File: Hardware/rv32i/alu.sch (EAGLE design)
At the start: 51 parts, among them IC1 SN74HCS86DR, IC10 SN74HCS86DR, IC11 SN74HCS86DR, IC12 SN74HCS86DR, IC13 SN74HCS86DR, IC14 SN74HCS86DR, IC15 SN74HCS86DR, IC16 SN74HCS86DR, IC17 SN74HCS86DR, IC18 SN74HCS86DR, IC19 SN74HCS86DR, IC2 SN74HCS86DR, IC20 SN74HCS86DR, IC21 SN74HCS86DR, IC22 SN74HCS86DR, IC23 SN74HCS86DR, IC24 SN74HCS86DR, IC25 SN74ACT08D, IC26 SN74ACT08D, IC27 SN74ACT08D, IC28 SN74ACT08D, IC29 SN74ACT08D, IC3 SN74HCS86DR, IC30 SN74ACT08D, IC31 SN74ACT08D, IC32 SN74ACT08D, IC33 SN74ACT08D, IC34 SN74ACT08D, IC35 SN74ACT08D, IC36 SN74ACT08D, IC37 SN74ACT08D, IC38 SN74ACT08D, IC39 SN74ACT08D, IC4 SN74HCS86DR, IC40 SN74ACT08D, IC41 SN74HCS32DR, IC42 SN74HCS32DR, IC43 SN74HCS32DR, IC44 SN74HCS32DR, IC45 SN74HCS32DR, IC46 SN74HCS32DR, IC47 SN74HCS32DR, IC48 SN74HCS32DR, IC5 SN74HCS86DR, IC6 SN74HCS86DR, IC7 SN74HCS86DR, IC8 SN74HCS86DR, IC9 SN74HCS86DR

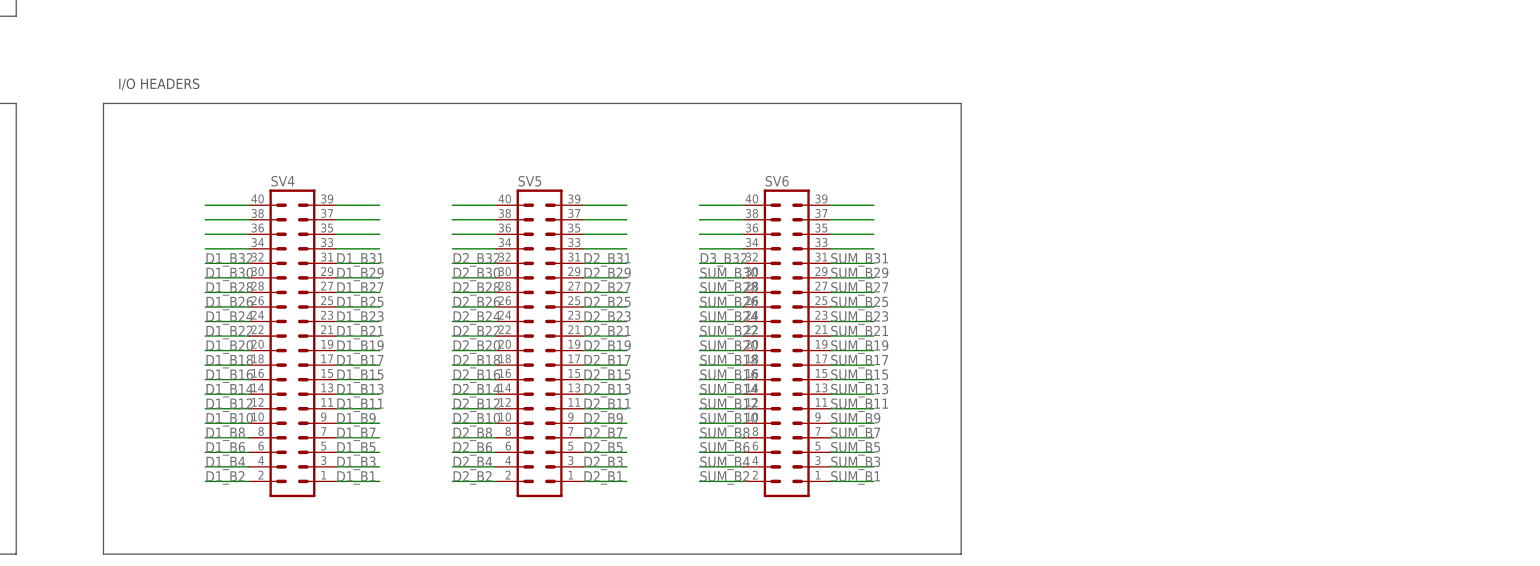
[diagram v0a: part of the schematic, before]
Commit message: Headers Changed
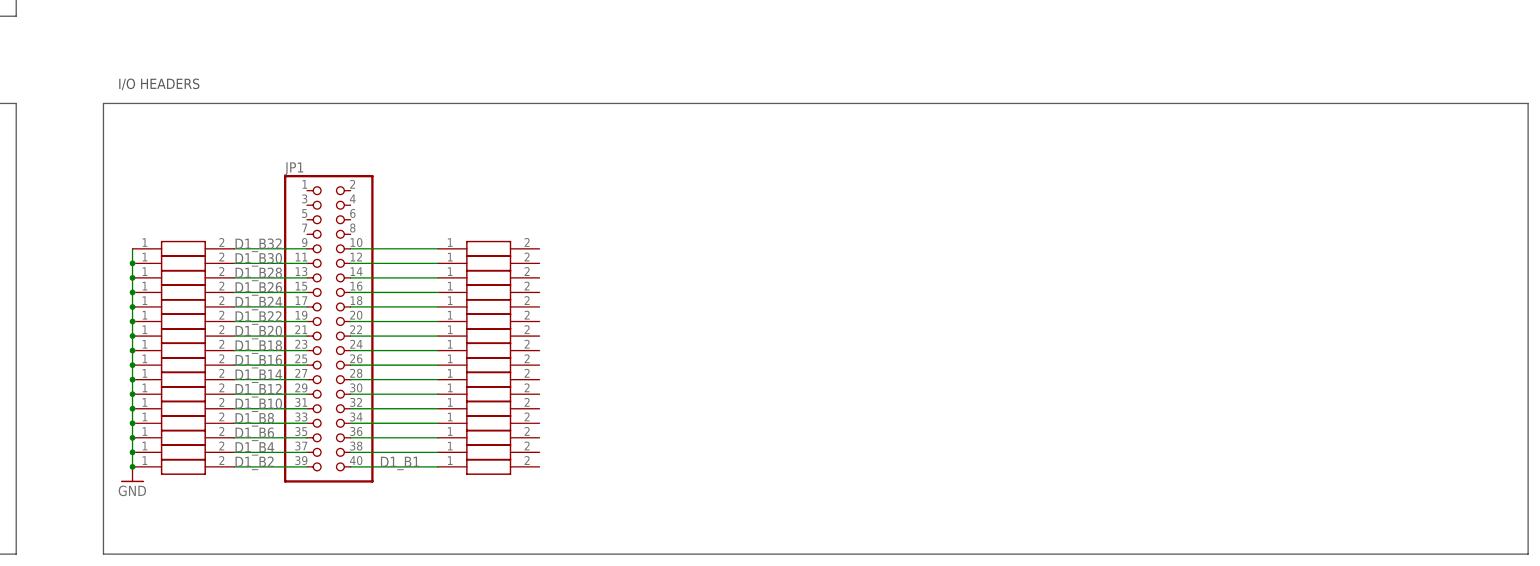
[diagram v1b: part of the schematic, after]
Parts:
- removed SV4, SV5, SV6: (no value), con-lstb:MA20-2
- added JP1: (no value), pinhead:PINHD-2X20
- added R1, R10, R11, R12, R13, R14, R15, R16, R17, R18, R19, R2, R20, R21, R22, R23, R24, R25, R26, R27, R28, R29, R3, R30, R31, R32, R4, R5, R6, R7, R8, R9: RC0603FR-0710KL, RC0603FR-0710KL:RC0603FR-0710KL
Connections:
- removed net B1_A0: SV4.33
- removed net D1_B34: SV4.34
- removed net D3_B32: SV6.32
- removed net N$569: SV4.38
- removed net N$570: SV4.36
- removed net N$587: SV4.37
- removed net N$588: SV4.35
- removed net N$607: SV4.39
- removed net N$608: SV4.40
- removed net N$609: SV5.38
- removed net N$610: SV5.36
- removed net N$611: SV5.34
- removed net N$627: SV5.37
- removed net N$628: SV5.35
- removed net N$629: SV5.33
- removed net N$647: SV5.39
- removed net N$648: SV5.40
- removed net N$649: SV6.38
- removed net N$650: SV6.36
- removed net N$651: SV6.34
- removed net N$667: SV6.37
- removed net N$668: SV6.35
- removed net N$669: SV6.33
- removed net N$687: SV6.39
- removed net N$688: SV6.40
- new net GND: R1.1, R10.1, R11.1, R12.1, R13.1, R14.1, R15.1, R16.1, R2.1, R3.1, R4.1, R5.1, R6.1, R7.1, R8.1, R9.1
- new net N$10: JP1.22, R26.1
- new net N$11: JP1.24, R25.1
- new net N$12: JP1.26, R17.1
- new net N$13: JP1.28, R18.1
- new net N$14: JP1.30, R19.1
- new net N$16: JP1.32, R20.1
- new net N$17: JP1.34, R22.1
- new net N$18: JP1.36, R21.1
- new net N$19: JP1.38, R23.1
- new net N$2: JP1.10, R31.1
- new net N$4: JP1.12, R32.1
- new net N$5: JP1.14, R30.1
- new net N$6: JP1.16, R29.1
- new net N$7: JP1.18, R28.1
- new net N$9: JP1.20, R27.1
- net D1_B1: now also JP1.40, R24.1; no longer SV4.1
- net D1_B10: now also JP1.31, R4.2; no longer SV4.10
- net D1_B11: no longer SV4.11
- net D1_B12: now also JP1.29, R3.2; no longer SV4.12
- net D1_B13: no longer SV4.13
- net D1_B14: now also JP1.27, R2.2; no longer SV4.14
- net D1_B15: no longer SV4.15
- net D1_B16: now also JP1.25, R1.2; no longer SV4.16
- net D1_B17: no longer SV4.17
- net D1_B18: now also JP1.23, R9.2; no longer SV4.18
- net D1_B19: no longer SV4.19
- net D1_B2: now also JP1.39, R8.2; no longer SV4.2
- net D1_B20: now also JP1.21, R10.2; no longer SV4.20
- net D1_B21: no longer SV4.21
- net D1_B22: now also JP1.19, R11.2; no longer SV4.22
- net D1_B23: no longer SV4.23
- net D1_B24: now also JP1.17, R12.2; no longer SV4.24
- net D1_B25: no longer SV4.25
- net D1_B26: now also JP1.15, R13.2; no longer SV4.26
- net D1_B27: no longer SV4.27
- net D1_B28: now also JP1.13, R14.2; no longer SV4.28
- net D1_B29: no longer SV4.29
- net D1_B3: no longer SV4.3
- net D1_B30: now also JP1.11, R16.2; no longer SV4.30
- net D1_B31: no longer SV4.31
- net D1_B32: now also JP1.9, R15.2; no longer SV4.32
- net D1_B4: now also JP1.37, R7.2; no longer SV4.4
- net D1_B5: no longer SV4.5
- net D1_B6: now also JP1.35, R5.2; no longer SV4.6
- net D1_B7: no longer SV4.7
- net D1_B8: now also JP1.33, R6.2; no longer SV4.8
- net D1_B9: no longer SV4.9
- net D2_B1: no longer SV5.1
- net D2_B10: no longer SV5.10
- net D2_B11: no longer SV5.11
- net D2_B12: no longer SV5.12
- net D2_B13: no longer SV5.13
- net D2_B14: no longer SV5.14
- net D2_B15: no longer SV5.15
- net D2_B16: no longer SV5.16
- net D2_B17: no longer SV5.17
- net D2_B18: no longer SV5.18
- net D2_B19: no longer SV5.19
- net D2_B2: no longer SV5.2
- net D2_B20: no longer SV5.20
- net D2_B21: no longer SV5.21
- net D2_B22: no longer SV5.22
- net D2_B23: no longer SV5.23
- net D2_B24: no longer SV5.24
- net D2_B25: no longer SV5.25
- net D2_B26: no longer SV5.26
- net D2_B27: no longer SV5.27
- net D2_B28: no longer SV5.28
- net D2_B29: no longer SV5.29
- net D2_B3: no longer SV5.3
- net D2_B30: no longer SV5.30
- net D2_B31: no longer SV5.31
- net D2_B32: no longer SV5.32
- net D2_B4: no longer SV5.4
- net D2_B5: no longer SV5.5
- net D2_B6: no longer SV5.6
- net D2_B7: no longer SV5.7
- net D2_B8: no longer SV5.8
- net D2_B9: no longer SV5.9
- net SUM_B1: no longer SV6.1
- net SUM_B10: no longer SV6.10
- net SUM_B11: no longer SV6.11
- net SUM_B12: no longer SV6.12
- net SUM_B13: no longer SV6.13
- net SUM_B14: no longer SV6.14
- net SUM_B15: no longer SV6.15
- net SUM_B16: no longer SV6.16
- net SUM_B17: no longer SV6.17
- net SUM_B18: no longer SV6.18
- net SUM_B19: no longer SV6.19
- net SUM_B2: no longer SV6.2
- net SUM_B20: no longer SV6.20
- net SUM_B21: no longer SV6.21
- net SUM_B22: no longer SV6.22
- net SUM_B23: no longer SV6.23
- net SUM_B24: no longer SV6.24
- net SUM_B25: no longer SV6.25
- net SUM_B26: no longer SV6.26
- net SUM_B27: no longer SV6.27
- net SUM_B28: no longer SV6.28
- net SUM_B29: no longer SV6.29
- net SUM_B3: no longer SV6.3
- net SUM_B30: no longer SV6.30
- net SUM_B31: no longer SV6.31
- net SUM_B4: no longer SV6.4
- net SUM_B5: no longer SV6.5
- net SUM_B6: no longer SV6.6
- net SUM_B7: no longer SV6.7
- net SUM_B8: no longer SV6.8
- net SUM_B9: no longer SV6.9

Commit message: ALU Headers & Timing Gates
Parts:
- added JP2, JP3, JP4, JP5, JP6: (no value), pinhead:PINHD-2X20
- added R33, R34, R35, R36, R37, R38, R39, R40, R41, R42, R43, R44, R45, R46, R47, R48, R49, R50, R51, R52, R53, R54, R55, R56, R57, R58, R59, R60, R61, R62, R63, R64: RC0603FR-0710KL, RC0603FR-0710KL:RC0603FR-0710KL
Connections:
- removed net N$10: JP1.22, R26.1
- removed net N$11: JP1.24, R25.1
- removed net N$12: JP1.26, R17.1
- removed net N$13: JP1.28, R18.1
- removed net N$14: JP1.30, R19.1
- removed net N$16: JP1.32, R20.1
- removed net N$17: JP1.34, R22.1
- removed net N$18: JP1.36, R21.1
- removed net N$19: JP1.38, R23.1
- removed net N$2: JP1.10, R31.1
- removed net N$4: JP1.12, R32.1
- removed net N$5: JP1.14, R30.1
- removed net N$6: JP1.16, R29.1
- removed net N$7: JP1.18, R28.1
- removed net N$9: JP1.20, R27.1
- new net D1_B0: JP2.5, JP3.5, R1.1
- new net D2_B0: JP1.5, JP4.5, R33.1
- new net SUM_B0: JP5.5, JP6.5
- new net VCC: JP1.1, JP1.2, JP1.39, JP1.40, JP2.1, JP2.2, JP2.39, JP2.40, JP3.1, JP3.2, JP3.39, JP3.40, JP4.1, JP4.2, JP4.39, JP4.40, JP5.1, JP5.2, JP5.39, JP5.40, JP6.1, JP6.2, JP6.39, JP6.40
- net D1_B1: now also JP2.7, JP3.7, R2.1; no longer JP1.40, R24.1
- net D1_B10: now also JP2.25, JP3.25, R11.1, R12.1; no longer JP1.31, R4.2
- net D1_B11: now also JP2.27, JP3.27
- net D1_B12: now also JP2.29, JP3.29, R13.1; no longer JP1.29, R3.2
- net D1_B13: now also JP2.31, JP3.31, R14.1
- net D1_B14: now also JP2.33, JP3.33, R15.1; no longer JP1.27, R2.2
- net D1_B15: now also JP2.35, JP3.35, R17.1
- net D1_B16: now also JP2.6, JP3.6, R16.1; no longer JP1.25, R1.2
- net D1_B17: now also JP2.8, JP3.8, R18.1
- net D1_B18: now also JP2.10, JP3.10, R19.1; no longer JP1.23, R9.2
- net D1_B19: now also JP2.12, JP3.12, R20.1
- net D1_B2: now also JP2.9, JP3.9, R3.1; no longer JP1.39, R8.2
- net D1_B20: now also JP2.14, JP3.14, R21.1; no longer JP1.21, R10.2
- net D1_B21: now also JP2.16, JP3.16, R22.1
- net D1_B22: now also JP2.18, JP3.18, R23.1; no longer JP1.19, R11.2
- net D1_B23: now also JP2.20, JP3.20, R24.1
- net D1_B24: now also JP2.22, JP3.22, R26.1; no longer JP1.17, R12.2
- net D1_B25: now also JP2.24, JP3.24, R25.1
- net D1_B26: now also JP2.26, JP3.26, R27.1; no longer JP1.15, R13.2
- net D1_B27: now also JP2.28, JP3.28, R28.1
- net D1_B28: now also JP2.30, JP3.30, R29.1; no longer JP1.13, R14.2
- net D1_B29: now also JP2.32, JP3.32, R30.1
- net D1_B3: now also JP2.11, JP3.11, R4.1
- net D1_B30: now also JP2.34, JP3.34, R31.1; no longer JP1.11, R16.2
- net D1_B31: now also JP2.36, JP3.36, R32.1
- net D1_B32: no longer JP1.9, R15.2
- net D1_B4: now also JP2.13, JP3.13, R5.1; no longer JP1.37, R7.2
- net D1_B5: now also JP2.15, JP3.15, R6.1
- net D1_B6: now also JP2.17, JP3.17, R7.1; no longer JP1.35, R5.2
- net D1_B7: now also JP2.19, JP3.19, R8.1
- net D1_B8: now also JP2.21, JP3.21, R9.1; no longer JP1.33, R6.2
- net D1_B9: now also JP2.23, JP3.23, R10.1
- net D2_B1: now also JP1.7, JP4.7, R34.1
- net D2_B10: now also JP1.25, JP4.25, R43.1
- net D2_B11: now also JP1.27, JP4.27, R44.1
- net D2_B12: now also JP1.29, JP4.29, R45.1
- net D2_B13: now also JP1.31, JP4.31, R46.1
- net D2_B14: now also JP1.33, JP4.33, R47.1
- net D2_B15: now also JP1.35, JP4.35, R49.1
- net D2_B16: now also JP1.6, JP4.6, R48.1
- net D2_B17: now also JP1.8, JP4.8, R50.1
- net D2_B18: now also JP1.10, JP4.10, R51.1
- net D2_B19: now also JP1.12, JP4.12, R52.1
- net D2_B2: now also JP1.9, JP4.9, R35.1
- net D2_B20: now also JP1.14, JP4.14, R53.1
- net D2_B21: now also JP1.16, JP4.16, R54.1
- net D2_B22: now also JP1.18, JP4.18, R55.1
- net D2_B23: now also JP1.20, JP4.20, R56.1, R58.1
- net D2_B24: now also JP1.22, JP4.22
- net D2_B25: now also JP1.24, JP4.24, R57.1
- net D2_B26: now also JP1.26, JP4.26, R59.1
- net D2_B27: now also JP1.28, JP4.28, R60.1
- net D2_B28: now also JP1.30, JP4.30, R61.1
- net D2_B29: now also JP1.32, JP1.34, JP4.32, JP4.34, R62.1
- net D2_B3: now also JP1.11, JP4.11, R36.1
- net D2_B30: now also R63.1
- net D2_B31: now also JP1.36, JP4.36, R64.1
- net D2_B4: now also JP1.13, JP4.13, R37.1
- net D2_B5: now also JP1.15, JP4.15, R38.1
- net D2_B6: now also JP1.17, JP4.17, R39.1
- net D2_B7: now also JP1.19, JP4.19, R40.1
- net D2_B8: now also JP1.21, JP4.21, R41.1
- net D2_B9: now also JP1.23, JP4.23, R42.1
- net GND: now also JP1.3, JP1.37, JP1.38, JP1.4, JP2.3, JP2.37, JP2.38, JP2.4, JP3.3, JP3.37, JP3.38, JP3.4, JP4.3, JP4.37, JP4.38, JP4.4, JP5.3, JP5.37, JP5.38, JP5.4, JP6.3, JP6.37, JP6.38, JP6.4, R1.2, R10.2, R11.2, R12.2, R13.2, R14.2, R15.2, R16.2, R17.2, R18.2, R19.2, R2.2, R20.2, R21.2, R22.2, R23.2, R24.2, R25.2, R26.2, R27.2, R28.2, R29.2, R3.2, R30.2, R31.2, R32.2, R33.2, R34.2, R35.2, R36.2, R37.2, R38.2, R39.2, R4.2, R40.2, R41.2, R42.2, R43.2, R44.2, R45.2, R46.2, R47.2, R48.2, R49.2, R5.2, R50.2, R51.2, R52.2, R53.2, R54.2, R55.2, R56.2, R57.2, R58.2, R59.2, R6.2, R60.2, R61.2, R62.2, R63.2, R64.2, R7.2, R8.2, R9.2; no longer R1.1, R10.1, R11.1, R12.1, R13.1, R14.1, R15.1, R16.1, R2.1, R3.1, R4.1, R5.1, R6.1, R7.1, R8.1, R9.1
- net SUM_B1: now also JP5.7, JP6.7
- net SUM_B10: now also JP5.25, JP6.25
- net SUM_B11: now also JP5.27, JP6.27
- net SUM_B12: now also JP5.29, JP6.29
- net SUM_B13: now also JP5.31, JP6.31
- net SUM_B14: now also JP5.33, JP6.33
- net SUM_B15: now also JP5.35, JP6.35
- net SUM_B16: now also JP5.6, JP6.6
- net SUM_B17: now also JP5.8, JP6.8
- net SUM_B18: now also JP5.10, JP6.10
- net SUM_B19: now also JP5.12, JP6.12
- net SUM_B2: now also JP5.9, JP6.9
- net SUM_B20: now also JP5.14, JP6.14
- net SUM_B21: now also JP5.16, JP6.16
- net SUM_B22: now also JP5.18, JP6.18
- net SUM_B23: now also JP5.20, JP6.20
- net SUM_B24: now also JP5.22, JP6.22
- net SUM_B25: now also JP5.24, JP6.24
- net SUM_B26: now also JP5.26, JP6.26
- net SUM_B27: now also JP5.28, JP6.28
- net SUM_B28: now also JP5.30, JP6.30
- net SUM_B29: now also JP5.32, JP5.34, JP6.32, JP6.34
- net SUM_B3: now also JP5.11, JP6.11
- net SUM_B31: now also JP5.36, JP6.36
- net SUM_B4: now also JP5.13, JP5.15, JP6.13, JP6.15
- net SUM_B6: now also JP5.17, JP6.17
- net SUM_B7: now also JP5.19, JP6.19
- net SUM_B8: now also JP5.21, JP6.21
- net SUM_B9: now also JP5.23, JP6.23
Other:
- note added: "PULL-DOWN RESISTORS"
- moved on the sheet: JP1

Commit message: Rename ALU Header Pins
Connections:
- removed net D1_B0: JP2.5, JP3.5, R1.1
- removed net D2_B0: JP1.5, JP4.5, R33.1
- removed net SUM_B0: JP5.5, JP6.5
- new net AND1_B33: IC47.3A
- net AND1_B32: no longer IC47.3A
- net D1_B1: now also JP2.5, JP3.5, R1.1; no longer JP2.7, JP3.7, R2.1
- net D1_B10: now also JP2.23, JP3.23, R10.1; no longer JP2.25, JP3.25, R11.1, R12.1
- net D1_B11: now also JP2.25, JP3.25, R11.1, R12.1; no longer JP2.27, JP3.27
- net D1_B12: now also JP2.27, JP3.27; no longer JP2.29, JP3.29, R13.1
- net D1_B13: now also JP2.29, JP3.29, R13.1; no longer JP2.31, JP3.31, R14.1
- net D1_B14: now also JP2.31, JP3.31, R14.1; no longer JP2.33, JP3.33, R15.1
- net D1_B15: now also JP2.33, JP3.33, R15.1; no longer JP2.35, JP3.35, R17.1
- net D1_B16: now also JP2.35, JP3.35, R17.1; no longer JP2.6, JP3.6, R16.1
- net D1_B17: now also JP2.6, JP3.6, R16.1; no longer JP2.8, JP3.8, R18.1
- net D1_B18: now also JP2.8, JP3.8, R18.1; no longer JP2.10, JP3.10, R19.1
- net D1_B19: now also JP2.10, JP3.10, R19.1; no longer JP2.12, JP3.12, R20.1
- net D1_B2: now also JP2.7, JP3.7, R2.1; no longer JP2.9, JP3.9, R3.1
- net D1_B20: now also JP2.12, JP3.12, R20.1; no longer JP2.14, JP3.14, R21.1
- net D1_B21: now also JP2.14, JP3.14, R21.1; no longer JP2.16, JP3.16, R22.1
- net D1_B22: now also JP2.16, JP3.16, R22.1; no longer JP2.18, JP3.18, R23.1
- net D1_B23: now also JP2.18, JP3.18, R23.1; no longer JP2.20, JP3.20, R24.1
- net D1_B24: now also JP2.20, JP3.20, R24.1; no longer JP2.22, JP3.22, R26.1
- net D1_B25: now also JP2.22, JP3.22, R26.1; no longer JP2.24, JP3.24, R25.1
- net D1_B26: now also JP2.24, JP3.24, R25.1; no longer JP2.26, JP3.26, R27.1
- net D1_B27: now also JP2.26, JP3.26, R27.1; no longer JP2.28, JP3.28, R28.1
- net D1_B28: now also JP2.28, JP3.28, R28.1; no longer JP2.30, JP3.30, R29.1
- net D1_B29: now also JP2.30, JP3.30, R29.1; no longer JP2.32, JP3.32, R30.1
- net D1_B3: now also JP2.9, JP3.9, R3.1; no longer JP2.11, JP3.11, R4.1
- net D1_B30: now also JP2.32, JP3.32, R30.1; no longer JP2.34, JP3.34, R31.1
- net D1_B31: now also JP2.34, JP3.34, R31.1; no longer JP2.36, JP3.36, R32.1
- net D1_B32: now also JP2.36, JP3.36, R32.1
- net D1_B4: now also JP2.11, JP3.11, R4.1; no longer JP2.13, JP3.13, R5.1
- net D1_B5: now also JP2.13, JP3.13, R5.1; no longer JP2.15, JP3.15, R6.1
- net D1_B6: now also JP2.15, JP3.15, R6.1; no longer JP2.17, JP3.17, R7.1
- net D1_B7: now also JP2.17, JP3.17, R7.1; no longer JP2.19, JP3.19, R8.1
- net D1_B8: now also JP2.19, JP3.19, R8.1; no longer JP2.21, JP3.21, R9.1
- net D1_B9: now also JP2.21, JP3.21, R9.1; no longer JP2.23, JP3.23, R10.1
- net D2_B1: now also JP1.5, JP4.5, R33.1; no longer JP1.7, JP4.7, R34.1
- net D2_B10: now also JP1.23, JP4.23, R42.1; no longer JP1.25, JP4.25, R43.1
- net D2_B11: now also JP1.25, JP4.25, R43.1; no longer JP1.27, JP4.27, R44.1
- net D2_B12: now also JP1.27, JP4.27, R44.1; no longer JP1.29, JP4.29, R45.1
- net D2_B13: now also JP1.29, JP4.29, R45.1; no longer JP1.31, JP4.31, R46.1
- net D2_B14: now also JP1.31, JP4.31, R46.1; no longer JP1.33, JP4.33, R47.1
- net D2_B15: now also JP1.33, JP4.33, R47.1; no longer JP1.35, JP4.35, R49.1
- net D2_B16: now also JP1.35, JP4.35, R49.1; no longer JP1.6, JP4.6, R48.1
- net D2_B17: now also JP1.6, JP4.6, R48.1; no longer JP1.8, JP4.8, R50.1
- net D2_B18: now also JP1.8, JP4.8, R50.1; no longer JP1.10, JP4.10, R51.1
- net D2_B19: now also JP1.10, JP4.10, R51.1; no longer JP1.12, JP4.12, R52.1
- net D2_B2: now also JP1.7, JP4.7, R34.1; no longer JP1.9, JP4.9, R35.1
- net D2_B20: now also JP1.12, JP4.12, R52.1; no longer JP1.14, JP4.14, R53.1
- net D2_B21: now also JP1.14, JP4.14, R53.1; no longer JP1.16, JP4.16, R54.1
- net D2_B22: now also JP1.16, JP4.16, R54.1; no longer JP1.18, JP4.18, R55.1
- net D2_B23: now also JP1.18, JP4.18, R55.1; no longer JP1.20, JP4.20, R56.1, R58.1
- net D2_B24: now also JP1.20, JP4.20, R56.1, R58.1; no longer JP1.22, JP4.22
- net D2_B25: now also JP1.22, JP4.22; no longer JP1.24, JP4.24, R57.1
- net D2_B26: now also JP1.24, JP4.24, R57.1; no longer JP1.26, JP4.26, R59.1
- net D2_B27: now also JP1.26, JP4.26, R59.1; no longer JP1.28, JP4.28, R60.1
- net D2_B28: now also JP1.28, JP4.28, R60.1; no longer JP1.30, JP4.30, R61.1
- net D2_B29: now also JP1.30, JP4.30, R61.1; no longer JP1.32, JP1.34, JP4.32, JP4.34, R62.1
- net D2_B3: now also JP1.9, JP4.9, R35.1; no longer JP1.11, JP4.11, R36.1
- net D2_B30: now also JP1.32, JP1.34, JP4.32, JP4.34, R62.1; no longer R63.1
- net D2_B31: now also R63.1; no longer JP1.36, JP4.36, R64.1
- net D2_B32: now also JP1.36, JP4.36, R64.1
- net D2_B4: now also JP1.11, JP4.11, R36.1; no longer JP1.13, JP4.13, R37.1
- net D2_B5: now also JP1.13, JP4.13, R37.1; no longer JP1.15, JP4.15, R38.1
- net D2_B6: now also JP1.15, JP4.15, R38.1; no longer JP1.17, JP4.17, R39.1
- net D2_B7: now also JP1.17, JP4.17, R39.1; no longer JP1.19, JP4.19, R40.1
- net D2_B8: now also JP1.19, JP4.19, R40.1; no longer JP1.21, JP4.21, R41.1
- net D2_B9: now also JP1.21, JP4.21, R41.1; no longer JP1.23, JP4.23, R42.1
- net SUM_B1: now also JP5.5, JP6.5; no longer JP5.7, JP6.7
- net SUM_B10: now also JP5.23, JP6.23; no longer JP5.25, JP6.25
- net SUM_B11: now also JP5.25, JP6.25; no longer JP5.27, JP6.27
- net SUM_B12: now also JP5.27, JP6.27; no longer JP5.29, JP6.29
- net SUM_B13: now also JP5.29, JP6.29; no longer JP5.31, JP6.31
- net SUM_B14: now also JP5.31, JP6.31; no longer JP5.33, JP6.33
- net SUM_B15: now also JP5.33, JP6.33; no longer JP5.35, JP6.35
- net SUM_B16: now also JP5.35, JP6.35; no longer JP5.6, JP6.6
- net SUM_B17: now also JP5.6, JP6.6; no longer JP5.8, JP6.8
- net SUM_B18: now also JP5.8, JP6.8; no longer JP5.10, JP6.10
- net SUM_B19: now also JP5.10, JP6.10; no longer JP5.12, JP6.12
- net SUM_B2: now also JP5.7, JP6.7; no longer JP5.9, JP6.9
- net SUM_B20: now also JP5.12, JP6.12; no longer JP5.14, JP6.14
- net SUM_B21: now also JP5.14, JP6.14; no longer JP5.16, JP6.16
- net SUM_B22: now also JP5.16, JP6.16; no longer JP5.18, JP6.18
- net SUM_B23: now also JP5.18, JP6.18; no longer JP5.20, JP6.20
- net SUM_B24: now also JP5.20, JP6.20; no longer JP5.22, JP6.22
- net SUM_B25: now also JP5.22, JP6.22; no longer JP5.24, JP6.24
- net SUM_B26: now also JP5.24, JP6.24; no longer JP5.26, JP6.26
- net SUM_B27: now also JP5.26, JP6.26; no longer JP5.28, JP6.28
- net SUM_B28: now also JP5.28, JP6.28; no longer JP5.30, JP6.30
- net SUM_B29: now also JP5.30, JP6.30; no longer JP5.32, JP5.34, JP6.32, JP6.34
- net SUM_B3: now also JP5.9, JP6.9; no longer JP5.11, JP6.11
- net SUM_B30: now also JP5.32, JP6.32
- net SUM_B31: now also JP5.34, JP6.34; no longer JP5.36, JP6.36
- net SUM_B32: now also JP5.36, JP6.36
- net SUM_B4: now also JP5.11, JP6.11; no longer JP5.13, JP5.15, JP6.13, JP6.15
- net SUM_B5: now also JP5.13, JP5.15, JP6.13, JP6.15
- net SUM_B6: no longer JP5.17, JP6.17
- net SUM_B7: now also JP5.17, JP6.17; no longer JP5.19, JP6.19
- net SUM_B8: now also JP5.19, JP6.19; no longer JP5.21, JP6.21
- net SUM_B9: now also JP5.21, JP6.21; no longer JP5.23, JP6.23
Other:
- moved on the sheet: IC42, IC43, IC44, IC45, IC46, IC47, IC48

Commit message: Capacitors
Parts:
- added C1, C10, C11, C12, C13, C14, C15, C16, C17, C18, C19, C2, C20, C21, C22, C23, C24, C3, C4, C5, C6, C7, C8, C9: CC0603KRX7R9BB104, CC0603KRX7R9BB104:CC0603KRX7R9BB104
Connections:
- new net N$2: C1.2, C10.2, C11.2, C12.2, C13.2, C14.2, C15.2, C16.2, C17.2, C18.2, C19.2, C2.2, C20.2, C21.2, C22.2, C23.2, C24.2, C3.2, C4.2, C5.2, C6.2, C7.2, C8.2, C9.2
- net GND: now also C1.1, C10.1, C11.1, C12.1, C13.1, C14.1, C15.1, C16.1, C17.1, C18.1, C19.1, C2.1, C20.1, C21.1, C22.1, C23.1, C24.1, C3.1, C4.1, C5.1, C6.1, C7.1, C8.1, C9.1
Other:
- note added: "Passive Components"
